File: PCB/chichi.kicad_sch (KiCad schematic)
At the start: 6 parts, among them U1 ESP32-C3_SUPERMINI_TH, U2 Charger_Module, U3 LiPo Battery

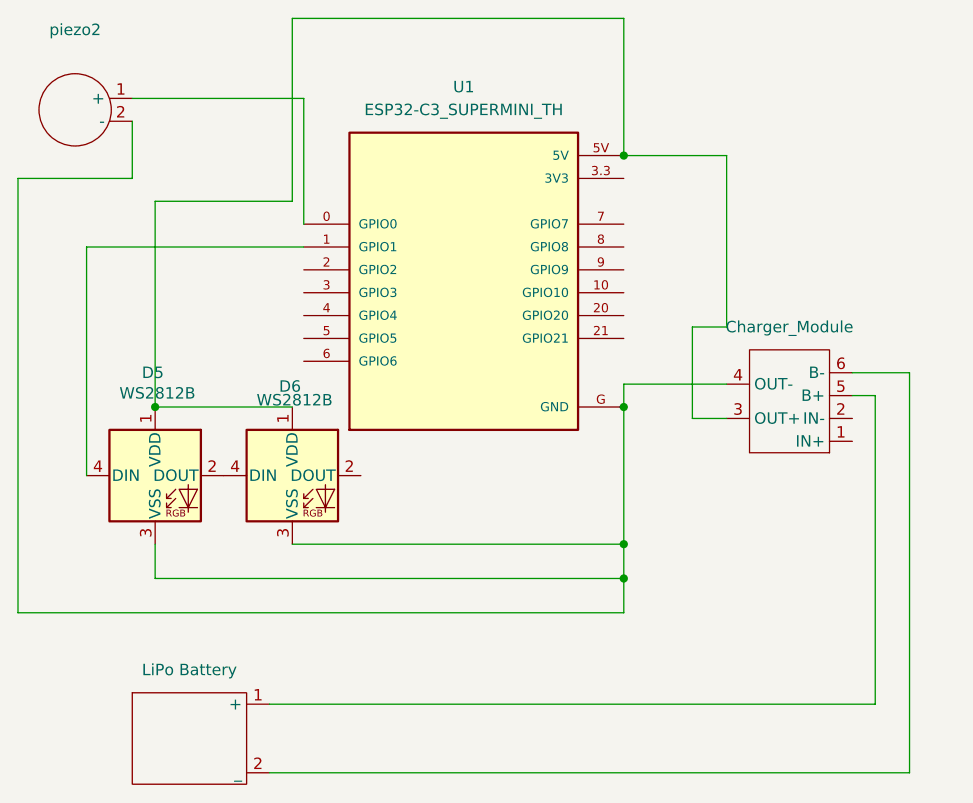
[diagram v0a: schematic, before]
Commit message: Add MT3608 Module
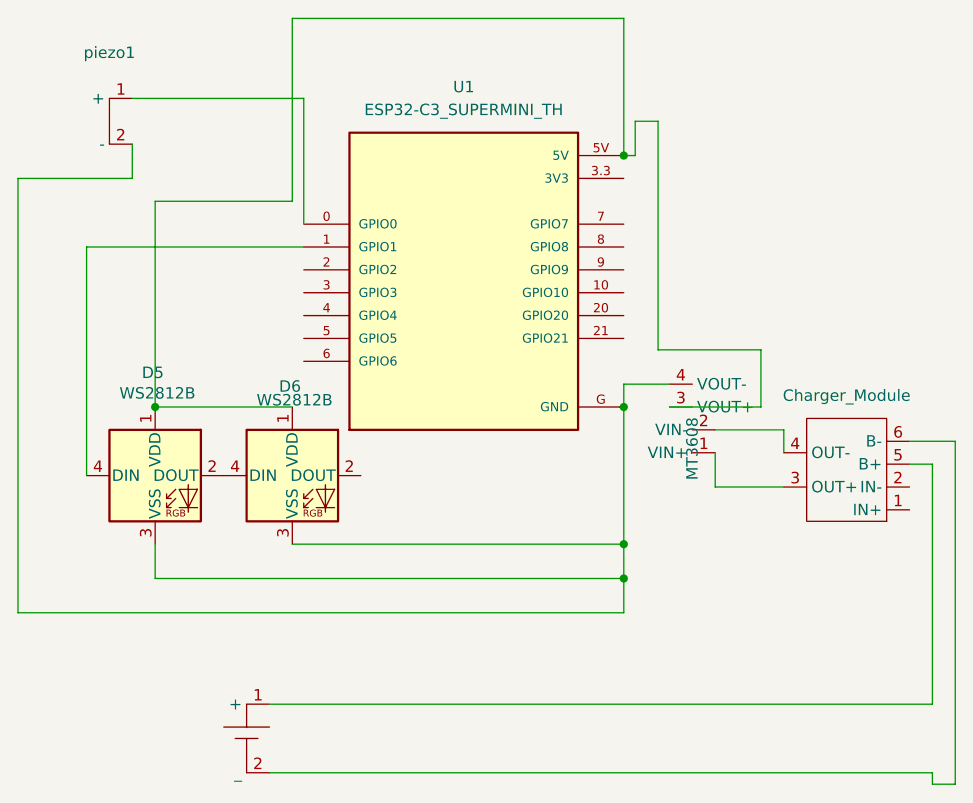
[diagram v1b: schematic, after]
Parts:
- removed piezo2: ~, charger:piezo, symbol chargerr:piezo
- added U4: MT3608, charger:MT3608 Boost Converter, symbol chargerr:MT3608_Boost_Converter
- added piezo1: ~, charger:piezo, symbol chargerr:piezo
- U3: value LiPo Battery -> ~
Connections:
- net at D5.1 (VDD), D6.1 (VDD), U1.5V: now also U4.3 (VOUT+); no longer U2.3 (OUT+)
- net at D5.3 (VSS), D6.3 (VSS), U1.G (GND): now also U4.4 (VOUT-), piezo1.2 (-); no longer U2.4 (OUT-)
- net at U1.0 (GPIO0): now also piezo1.1 (+)
- new net: U2.3 (OUT+), U4.1 (VIN+)
- new net: U2.4 (OUT-), U4.2 (VIN-)
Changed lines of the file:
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@@
-	(wire
-		(pts
-			(xy 255.27 95.25) (xy 251.46 95.25)
-		)
-		(stroke
-			(width 0)
-			(type default)
-		)
-	)
 	(wire
 		(pts
@@
 	(wire
 		(pts
-			(xy 255.27 76.2) (xy 255.27 95.25)
-		)
-		(stroke
-			(width 0)
-			(type default)
-		)
-	)
-	(wire
-		(pts
-			(xy 275.59 100.33) (xy 269.24 100.33)
+			(xy 189.23 74.93) (xy 189.23 78.74)
 		)
 		(stroke
@@
 	(wire
 		(pts
-			(xy 189.23 72.39) (xy 189.23 78.74)
-		)
-		(stroke
-			(width 0)
-			(type default)
-		)
-	)
-	(wire
-		(pts
 			(xy 176.53 127) (xy 243.84 127)
 		)
@@
 	(wire
 		(pts
-			(xy 251.46 105.41) (xy 255.27 105.41)
+			(xy 261.62 106.68) (xy 261.62 109.22)
 		)
 		(stroke
@@
 	(wire
 		(pts
-			(xy 271.78 137.16) (xy 271.78 102.87)
-		)
-		(stroke
-			(width 0)
-			(type default)
-		)
-	)
-	(wire
-		(pts
-			(xy 255.27 101.6) (xy 243.84 101.6)
+			(xy 247.65 72.39) (xy 245.11 72.39)
+		)
+		(stroke
+			(width 0)
+			(type default)
+		)
+	)
+	(wire
+		(pts
+			(xy 278.13 137.16) (xy 278.13 110.49)
+		)
+		(stroke
+			(width 0)
+			(type default)
+		)
+	)
+	(wire
+		(pts
+			(xy 248.92 104.14) (xy 259.08 104.14)
+		)
+		(stroke
+			(width 0)
+			(type default)
+		)
+	)
+	(wire
+		(pts
+			(xy 275.59 107.95) (xy 280.67 107.95)
+		)
+		(stroke
+			(width 0)
+			(type default)
+		)
+	)
+	(wire
+		(pts
+			(xy 275.59 110.49) (xy 278.13 110.49)
+		)
+		(stroke
+			(width 0)
+			(type default)
+		)
+	)
+	(wire
+		(pts
+			(xy 254 113.03) (xy 261.62 113.03)
 		)
 		(stroke
@@
 	(wire
 		(pts
-			(xy 204.47 144.78) (xy 275.59 144.78)
+			(xy 278.13 146.05) (xy 280.67 146.05)
+		)
+		(stroke
+			(width 0)
+			(type default)
+		)
+	)
+	(wire
+		(pts
+			(xy 245.11 76.2) (xy 243.84 76.2)
+		)
+		(stroke
+			(width 0)
+			(type default)
+		)
+	)
+	(wire
+		(pts
+			(xy 243.84 101.6) (xy 248.92 101.6)
+		)
+		(stroke
+			(width 0)
+			(type default)
+		)
+	)
+	(wire
+		(pts
+			(xy 254 109.22) (xy 254 113.03)
+		)
+		(stroke
+			(width 0)
+			(type default)
+		)
+	)
+	(wire
+		(pts
+			(xy 247.65 72.39) (xy 247.65 97.79)
 		)
 		(stroke
@@
 	(wire
 		(pts
-			(xy 204.47 137.16) (xy 271.78 137.16)
+			(xy 204.47 137.16) (xy 278.13 137.16)
 		)
 		(stroke
@@
 	(wire
 		(pts
-			(xy 271.78 102.87) (xy 269.24 102.87)
-		)
-		(stroke
-			(width 0)
-			(type default)
-		)
-	)
-	(wire
-		(pts
-			(xy 275.59 144.78) (xy 275.59 100.33)
+			(xy 280.67 146.05) (xy 280.67 107.95)
 		)
 		(stroke
@@
 	(wire
 		(pts
-			(xy 251.46 95.25) (xy 251.46 105.41)
-		)
-		(stroke
-			(width 0)
-			(type default)
-		)
-	)
-	(wire
-		(pts
-			(xy 255.27 76.2) (xy 243.84 76.2)
+			(xy 245.11 72.39) (xy 245.11 76.2)
+		)
+		(stroke
+			(width 0)
+			(type default)
+		)
+	)
+	(wire
+		(pts
+			(xy 259.08 97.79) (xy 247.65 97.79)
 		)
 		(stroke
@@
 	(wire
 		(pts
+			(xy 254 106.68) (xy 261.62 106.68)
+		)
+		(stroke
+			(width 0)
+			(type default)
+		)
+	)
+	(wire
+		(pts
 			(xy 208.28 69.85) (xy 208.28 83.82)
 		)
@@
 		(pts
 			(xy 191.77 119.38) (xy 191.77 123.19)
+		)
+		(stroke
+			(width 0)
+			(type default)
+		)
+	)
+	(wire
+		(pts
+			(xy 278.13 144.78) (xy 204.47 144.78)
+		)
+		(stroke
+			(width 0)
+			(type default)
+		)
+	)
+	(wire
+		(pts
+			(xy 259.08 104.14) (xy 259.08 97.79)
+		)
+		(stroke
+			(width 0)
+			(type default)
+		)
+	)
+	(wire
+		(pts
+			(xy 278.13 146.05) (xy 278.13 144.78)
 		)
 		(stroke
@@
 			)
 		)
-		(property "Value" "LiPo Battery"
-			(at 195.58 133.35 0)
+		(property "Value" "~"
+			(at 201.93 134.62 0)
 			(effects
 				(font
@@
 				(path "/7445f0f2-6d11-4fb0-a479-d765a424d1f2"
 					(reference "U3")
+					(unit 1)
+				)
+			)
+		)
+	)
+	(symbol
+		(lib_id "chargerr:piezo")
+		(at 182.88 68.58 0)
+		(unit 1)
+		(exclude_from_sim no)
+		(in_bom yes)
+		(on_board yes)
+		(dnp no)
+		(fields_autoplaced yes)
+		(property "Reference" "piezo1"
+			(at 186.69 64.77 0)
+			(effects
+				(font
+					(size 1.27 1.27)
+				)
+			)
+		)
+		(property "Value" "~"
+			(at 186.69 67.31 0)
+			(effects
+				(font
+					(size 1.27 1.27)
+				)
+			)
+		)
+		(property "Footprint" "charger:piezo"
+			(at 182.88 68.58 0)
+			(effects
+				(font
+					(size 1.27 1.27)
+				)
+				(hide yes)
+			)
+		)
+		(property "Datasheet" ""
+			(at 182.88 68.58 0)
+			(effects
+				(font
+					(size 1.27 1.27)
+				)
+				(hide yes)
+			)
+		)
+		(property "Description" ""
+			(at 182.88 68.58 0)
+			(effects
+				(font
+					(size 1.27 1.27)
+				)
+				(hide yes)
+			)
+		)
+		(pin "2"
+		)
+		(pin "1"
+		)
+		(instances
+			(project ""
+				(path "/7445f0f2-6d11-4fb0-a479-d765a424d1f2"
+					(reference "piezo1")
 					(unit 1)
 				)
@@
 	(symbol
 		(lib_id "chargerr:TP4056_Module")
-		(at 265.43 107.95 180)
+		(at 271.78 115.57 180)
 		(unit 1)
 		(exclude_from_sim no)
@@
 		(fields_autoplaced yes)
 		(property "Reference" "U2"
-			(at 265.43 107.95 0)
+			(at 271.78 115.57 0)
 			(effects
 				(font
@@
 		)
 		(property "Value" "Charger_Module"
-			(at 262.255 95.25 0)
+			(at 268.605 102.87 0)
 			(effects
 				(font
@@
 		)
 		(property "Footprint" "charger:TP4056-18650"
-			(at 265.43 107.95 0)
+			(at 271.78 115.57 0)
 			(effects
 				(font
@@
 		)
 		(property "Datasheet" ""
-			(at 265.43 107.95 0)
+			(at 271.78 115.57 0)
 			(effects
 				(font
@@
 		)
 		(property "Description" ""
-			(at 265.43 107.95 0)
+			(at 271.78 115.57 0)
 			(effects
 				(font
@@
 	)
 	(symbol
-		(lib_name "piezo_1")
-		(lib_id "chargerr:piezo")
-		(at 182.88 66.04 0)
+		(lib_id "chargerr:MT3608_Boost_Converter")
+		(at 251.46 110.49 180)
 		(unit 1)
 		(exclude_from_sim no)
@@
 		(on_board yes)
 		(dnp no)
-		(fields_autoplaced yes)
-		(property "Reference" "piezo2"
-			(at 182.88 62.23 0)
-			(effects
-				(font
-					(size 1.27 1.27)
-				)
-			)
-		)
-		(property "Value" "~"
-			(at 182.88 64.77 0)
-			(effects
-				(font
-					(size 1.27 1.27)
-				)
-			)
-		)
-		(property "Footprint" "charger:piezo"
-			(at 182.88 66.04 0)
+		(property "Reference" "U4"
+			(at 251.46 110.49 0)
+			(effects
+				(font
+					(size 1.27 1.27)
+				)
+				(hide yes)
+			)
+		)
+		(property "Value" "MT3608"
+			(at 251.46 112.268 90)
+			(effects
+				(font
+					(size 1.27 1.27)
+				)
+				(justify right)
+			)
+		)
+		(property "Footprint" "charger:MT3608 Boost Converter"
+			(at 251.46 110.49 0)
 			(effects
 				(font
@@
 		)
 		(property "Datasheet" ""
-			(at 182.88 66.04 0)
+			(at 251.46 110.49 0)
 			(effects
 				(font
@@
 		)
 		(property "Description" ""
-			(at 182.88 66.04 0)
-			(effects
-				(font
-					(size 1.27 1.27)
-				)
-				(hide yes)
-			)
+			(at 251.46 110.49 0)
+			(effects
+				(font
+					(size 1.27 1.27)
+				)
+				(hide yes)
+			)
+		)
+		(pin "2"
+		)
+		(pin "3"
+		)
+		(pin "4"
 		)
 		(pin "1"
-		)
-		(pin "2"
 		)
 		(instances
 			(project ""
 				(path "/7445f0f2-6d11-4fb0-a479-d765a424d1f2"
-					(reference "piezo2")
+					(reference "U4")
 					(unit 1)
 				)
